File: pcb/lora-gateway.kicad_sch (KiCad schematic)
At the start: 18 parts, among them J1 USB_B_Micro, J2 Conn_01x06, J3 Conn_01x06, J4 Conn_Coaxial, J5 AVR-JTAG-10, J6 AVR-ISP-6, SW1 SW_Push, U1 RFM95W-868S2, U2 ATmega2560-16A, U3 LM1117-3.3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

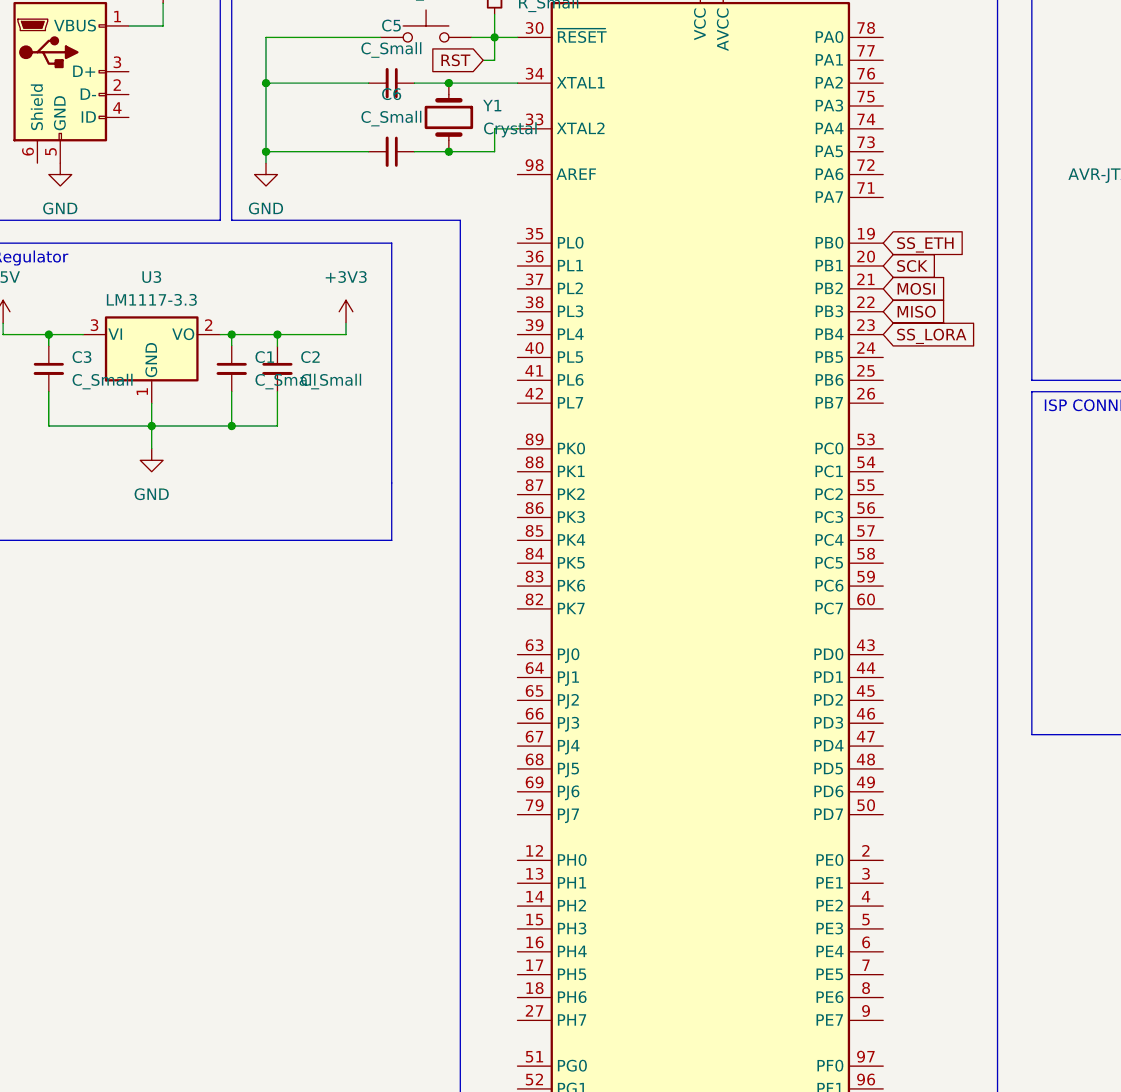
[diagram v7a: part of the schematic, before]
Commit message: add leds
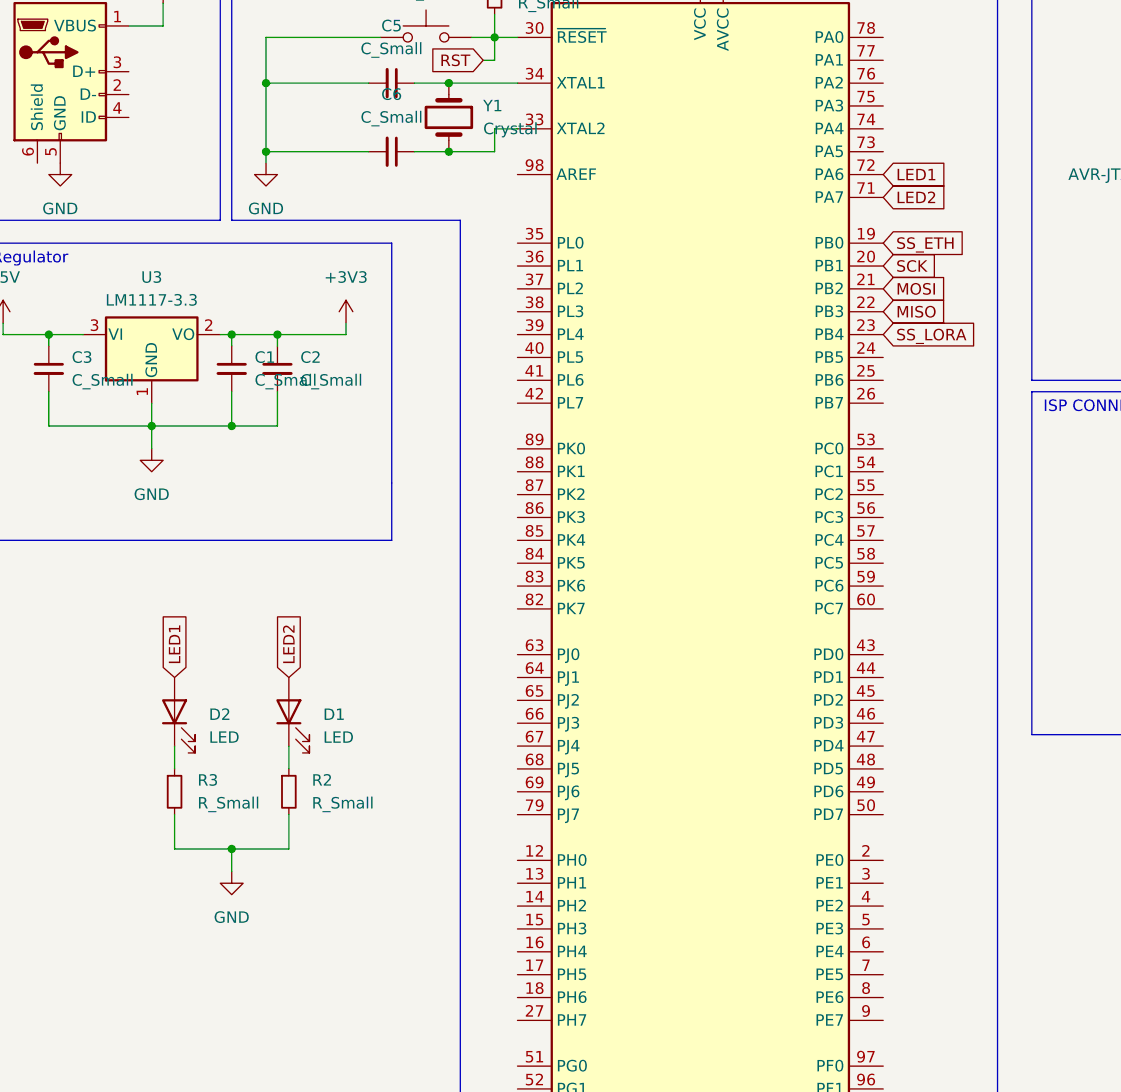
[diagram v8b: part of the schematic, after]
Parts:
- added D1, D2: LED, LED_SMD:LED_0603_1608Metric, symbol Device:LED
- added R2, R3: R_Small, Resistor_SMD:R_0603_1608Metric, symbol Device:R_Small
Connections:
- net GND: now also R2.2, R3.2
- net LED2: now reaches U2.71 (PA7)
- net LED2: now also D1.2 (A)
- net LED1: now reaches U2.72 (PA6)
- net LED1: now also D2.2 (A)
- new net: D2.1 (K), R3.1
- new net: D1.1 (K), R2.1
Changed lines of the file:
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@@
   (junction (at 21.59 64.77) (diameter 0) (color 0 0 0 0)
   )
+  (junction (at 41.91 121.92) (diameter 0) (color 0 0 0 0)
+  )
+  (wire (pts (xy 48.26 110.49) (xy 48.26 113.03))
+    (stroke (width 0) (type default))
+  )
   (wire (pts (xy 96.52 21.59) (xy 96.52 22.86))
     (stroke (width 0) (type default))
@@
     (stroke (width 0) (type default))
   )
+  (wire (pts (xy 41.91 121.92) (xy 48.26 121.92))
+    (stroke (width 0) (type default))
+  )
   (wire (pts (xy 209.55 26.67) (xy 205.74 26.67))
     (stroke (width 0) (type default))
@@
     (stroke (width 0) (type default))
   )
+  (wire (pts (xy 35.56 121.92) (xy 35.56 118.11))
+    (stroke (width 0) (type default))
+  )
   (wire (pts (xy 16.51 63.5) (xy 16.51 64.77))
     (stroke (width 0) (type default))
@@
     (stroke (width 0) (type default))
   )
+  (wire (pts (xy 41.91 124.46) (xy 41.91 121.92))
+    (stroke (width 0) (type default))
+  )
   (wire (pts (xy 45.72 31.75) (xy 45.72 36.83))
     (stroke (width 0) (type default))
@@
     (stroke (width 0) (type default))
   )
+  (wire (pts (xy 35.56 110.49) (xy 35.56 113.03))
+    (stroke (width 0) (type default))
+  )
   (polyline (pts (xy 40.64 15.24) (xy 15.24 15.24))
     (stroke (width 0) (type default))
@@
     (stroke (width 0) (type default))
   )
+  (wire (pts (xy 41.91 121.92) (xy 35.56 121.92))
+    (stroke (width 0) (type default))
+  )
   (polyline (pts (xy 262.89 74.93) (xy 262.89 15.24))
     (stroke (width 0) (type default))
@@
   )
   (wire (pts (xy 214.63 96.52) (xy 214.63 93.98))
+    (stroke (width 0) (type default))
+  )
+  (wire (pts (xy 48.26 118.11) (xy 48.26 121.92))
     (stroke (width 0) (type default))
   )
@@
     )
   )
+  (global_label "LED2" (shape input) (at 114.3 49.53 0) (fields_autoplaced)
+    (effects (font (size 1.27 1.27)) (justify left))
+    (property "Intersheetrefs" "${INTERSHEET_REFS}" (at 121.9418 49.53 0)
+      (effects (font (size 1.27 1.27)) (justify left) hide)
+    )
+  )
   (global_label "TDI" (shape input) (at 170.18 50.8 0) (fields_autoplaced)
     (effects (font (size 1.27 1.27)) (justify left))
@@
     (effects (font (size 1.27 1.27)) (justify left))
     (property "Intersheetrefs" "${INTERSHEET_REFS}" (at 178.1847 92.71 0)
+      (effects (font (size 1.27 1.27)) (justify left) hide)
+    )
+  )
+  (global_label "LED2" (shape input) (at 48.26 102.87 90) (fields_autoplaced)
+    (effects (font (size 1.27 1.27)) (justify left))
+    (property "Intersheetrefs" "${INTERSHEET_REFS}" (at 48.26 95.2282 90)
       (effects (font (size 1.27 1.27)) (justify left) hide)
     )
@@
     )
   )
+  (global_label "LED1" (shape input) (at 35.56 102.87 90) (fields_autoplaced)
+    (effects (font (size 1.27 1.27)) (justify left))
+    (property "Intersheetrefs" "${INTERSHEET_REFS}" (at 35.56 95.2282 90)
+      (effects (font (size 1.27 1.27)) (justify left) hide)
+    )
+  )
   (global_label "MISO" (shape input) (at 114.3 62.23 0) (fields_autoplaced)
     (effects (font (size 1.27 1.27)) (justify left))
@@
     (effects (font (size 1.27 1.27)) (justify left))
     (property "Intersheetrefs" "${INTERSHEET_REFS}" (at 124.1189 54.61 0)
+      (effects (font (size 1.27 1.27)) (justify left) hide)
+    )
+  )
+  (global_label "LED1" (shape input) (at 114.3 46.99 0) (fields_autoplaced)
+    (effects (font (size 1.27 1.27)) (justify left))
+    (property "Intersheetrefs" "${INTERSHEET_REFS}" (at 121.9418 46.99 0)
       (effects (font (size 1.27 1.27)) (justify left) hide)
     )
@@
     )
   )
+  (symbol (lib_id "power:GND") (at 41.91 124.46 0) (unit 1)
+    (in_bom yes) (on_board yes) (dnp no) (fields_autoplaced)
+    (property "Reference" "#PWR021" (at 41.91 130.81 0)
+      (effects (font (size 1.27 1.27)) hide)
+    )
+    (property "Value" "GND" (at 41.91 129.54 0)
+      (effects (font (size 1.27 1.27)))
+    )
+    (property "Footprint" "" (at 41.91 124.46 0)
+      (effects (font (size 1.27 1.27)) hide)
+    )
+    (property "Datasheet" "" (at 41.91 124.46 0)
+      (effects (font (size 1.27 1.27)) hide)
+    )
+    (pin "1")
+    (instances
+      (project "lora-gateway"
+        (path "/5fd0eb65-7f10-4bbb-b642-b528dcb1ea0e"
+          (reference "#PWR021") (unit 1)
+        )
+      )
+    )
+  )
   (symbol (lib_id "Device:C_Small") (at 212.09 26.67 90) (unit 1)
     (in_bom yes) (on_board yes) (dnp no) (fields_autoplaced)
@@
     )
   )
+  (symbol (lib_id "Device:R_Small") (at 35.56 115.57 0) (unit 1)
+    (in_bom yes) (on_board yes) (dnp no) (fields_autoplaced)
+    (property "Reference" "R3" (at 38.1 114.3 0)
+      (effects (font (size 1.27 1.27)) (justify left))
+    )
+    (property "Value" "R_Small" (at 38.1 116.84 0)
+      (effects (font (size 1.27 1.27)) (justify left))
+    )
+    (property "Footprint" "Resistor_SMD:R_0603_1608Metric" (at 35.56 115.57 0)
+      (effects (font (size 1.27 1.27)) hide)
+    )
+    (property "Datasheet" "~" (at 35.56 115.57 0)
+      (effects (font (size 1.27 1.27)) hide)
+    )
+    (pin "1")
+    (pin "2")
+    (instances
+      (project "lora-gateway"
+        (path "/5fd0eb65-7f10-4bbb-b642-b528dcb1ea0e"
+          (reference "R3") (unit 1)
+        )
+      )
+    )
+  )
   (symbol (lib_id "power:+5V") (at 34.29 27.94 0) (unit 1)
     (in_bom yes) (on_board yes) (dnp no) (fields_autoplaced)
@@
     )
   )
+  (symbol (lib_id "Device:R_Small") (at 48.26 115.57 0) (unit 1)
+    (in_bom yes) (on_board yes) (dnp no) (fields_autoplaced)
+    (property "Reference" "R2" (at 50.8 114.3 0)
+      (effects (font (size 1.27 1.27)) (justify left))
+    )
+    (property "Value" "R_Small" (at 50.8 116.84 0)
+      (effects (font (size 1.27 1.27)) (justify left))
+    )
+    (property "Footprint" "Resistor_SMD:R_0603_1608Metric" (at 48.26 115.57 0)
+      (effects (font (size 1.27 1.27)) hide)
+    )
+    (property "Datasheet" "~" (at 48.26 115.57 0)
+      (effects (font (size 1.27 1.27)) hide)
+    )
+    (pin "1")
+    (pin "2")
+    (instances
+      (project "lora-gateway"
+        (path "/5fd0eb65-7f10-4bbb-b642-b528dcb1ea0e"
+          (reference "R2") (unit 1)
+        )
+      )
+    )
+  )
   (symbol (lib_id "power:GND") (at 22.86 45.72 0) (unit 1)
     (in_bom yes) (on_board yes) (dnp no) (fields_autoplaced)
@@
         (path "/5fd0eb65-7f10-4bbb-b642-b528dcb1ea0e"
           (reference "C6") (unit 1)
+        )
+      )
+    )
+  )
+  (symbol (lib_id "Device:LED") (at 35.56 106.68 90) (unit 1)
+    (in_bom yes) (on_board yes) (dnp no) (fields_autoplaced)
+    (property "Reference" "D2" (at 39.37 106.9975 90)
+      (effects (font (size 1.27 1.27)) (justify right))
+    )
+    (property "Value" "LED" (at 39.37 109.5375 90)
+      (effects (font (size 1.27 1.27)) (justify right))
+    )
+    (property "Footprint" "LED_SMD:LED_0603_1608Metric" (at 35.56 106.68 0)
+      (effects (font (size 1.27 1.27)) hide)
+    )
+    (property "Datasheet" "~" (at 35.56 106.68 0)
+      (effects (font (size 1.27 1.27)) hide)
+    )
+    (pin "1")
+    (pin "2")
+    (instances
+      (project "lora-gateway"
+        (path "/5fd0eb65-7f10-4bbb-b642-b528dcb1ea0e"
+          (reference "D2") (unit 1)
         )
       )
@@
         )
       )
+    )
+  )
+  (symbol (lib_id "Device:LED") (at 48.26 106.68 90) (unit 1)
+    (in_bom yes) (on_board yes) (dnp no) (fields_autoplaced)
+    (property "Reference" "D1" (at 52.07 106.9975 90)
+      (effects (font (size 1.27 1.27)) (justify right))
+    )
+    (property "Value" "LED" (at 52.07 109.5375 90)
+      (effects (font (size 1.27 1.27)) (justify right))
+    )
+    (property "Footprint" "LED_SMD:LED_0603_1608Metric" (at 48.26 106.68 0)
+      (effects (font (size 1.27 1.27)) hide)
+    )
+    (property "Datasheet" "~" (at 48.26 106.68 0)
+      (effects (font (size 1.27 1.27)) hide)
+    )
+    (pin "1")
+    (pin "2")
+    (instances
+      (project "lora-gateway"
+        (path "/5fd0eb65-7f10-4bbb-b642-b528dcb1ea0e"
+          (reference "D1") (unit 1)
+        )
+      )
